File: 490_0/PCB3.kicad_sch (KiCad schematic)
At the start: 7 parts, among them J13 S2B-ZR, J14 Conn_01x08, J22 2000-1-1-20-00-BK, J8 0522711579

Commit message: Changed 8conn and BOM update
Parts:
- J13: footprint S2B-XH-A:JST_S2B-XH-A -> *CapStone*:CONN_S2B-ZR_JST
- J14: footprint *CapStone*:CONN_S8B-XH-A_JST -> *CapStone*:CONN_S08B-XASK-1_JST; Digikey Link https://www.digikey.ca/en/products/detail/jst-sales-america-inc/S8B-XH-A/1651023 -> https://www.digikey.ca/en/products/detail/jst-sales-america-inc/s08b-xask-1/2621356; Manufacturer Part S8B-XH-A -> S08B-XASK-1; Package (none) -> Bulk; Price 0.33 -> 0.81; Supplier P/N 455-S8B-XH-A-ND -> 455-S08B-XASK-1-ND; Type Through Hole -> Through Hole, Right Angle
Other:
- note added: "Camera CSI Connector 1mm pitch, 15-pin FFC"
- note removed: "Camera CSI Connector 0.5mm pitch, 15-pin FFC"
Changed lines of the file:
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@@
 		)
 	)
-	(text "Camera CSI Connector \n0.5mm pitch, 15-pin FFC\n"
+	(text "Camera CSI Connector \n1mm pitch, 15-pin FFC\n"
 		(exclude_from_sim no)
 		(at 33.782 74.168 0)
@@
 			)
 		)
-		(property "Footprint" "S2B-XH-A:JST_S2B-XH-A"
+		(property "Footprint" "*CapStone*:CONN_S2B-ZR_JST"
 			(at 33.655 57.785 0)
 			(effects
@@
 			)
 		)
-		(property "Footprint" "*CapStone*:CONN_S8B-XH-A_JST"
+		(property "Footprint" "*CapStone*:CONN_S08B-XASK-1_JST"
 			(at 198.12 28.575 0)
 			(effects
@@
 			)
 		)
-		(property "Datasheet" "kicad-embed://B3B-XH-A.pdf"
+		(property "Datasheet" "kicad-embed://eXA-WB-new.pdf"
 			(at 198.12 35.56 0)
 			(effects
@@
 			)
 		)
-		(property "Digikey Link" "https://www.digikey.ca/en/products/detail/jst-sales-america-inc/S8B-XH-A/1651023"
+		(property "Digikey Link" "https://www.digikey.ca/en/products/detail/jst-sales-america-inc/s08b-xask-1/2621356"
 			(at 198.12 40.64 0)
 			(effects
@@
 			)
 		)
-		(property "Manufacturer Part" "S8B-XH-A"
+		(property "Manufacturer Part" "S08B-XASK-1"
 			(at 198.12 40.64 0)
 			(effects
@@
 			)
 		)
-		(property "Price" "0.33"
+		(property "Price" "0.81"
 			(at 198.12 40.64 0)
 			(effects
@@
 			)
 		)
-		(property "Supplier P/N" "455-S8B-XH-A-ND"
+		(property "Supplier P/N" "455-S08B-XASK-1-ND"
 			(at 198.12 40.64 0)
 			(effects
@@
 			)
 		)
-		(property "Type" "Through Hole"
+		(property "Type" "Through Hole, Right Angle"
 			(at 198.12 40.64 0)
 			(effects
@@
 			(at 198.12 40.64 0)
 			(effects
+				(font
+					(size 1.27 1.27)
+				)
+				(hide yes)
+			)
+		)
+		(property "Package" "Bulk"
+			(at 198.12 40.64 0)
+			(effects

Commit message: LED names + 5V routing through ESD + renamed ESD chips to "U"
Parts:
- renumbered CR6 to U15
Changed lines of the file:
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@@
 		(dnp no)
 		(fields_autoplaced yes)
-		(property "Reference" "CR6"
+		(property "Reference" "U15"
 			(at 73.66 121.92 0)
 			(effects
@@
 			(project ""
 				(path "/365a82ed-827d-43e1-aa2f-b98221c4179c/a8971e06-9d2b-4df6-83ab-783791bb1c3f"
-					(reference "CR6")
+					(reference "U15")
 					(unit 1)
 				)

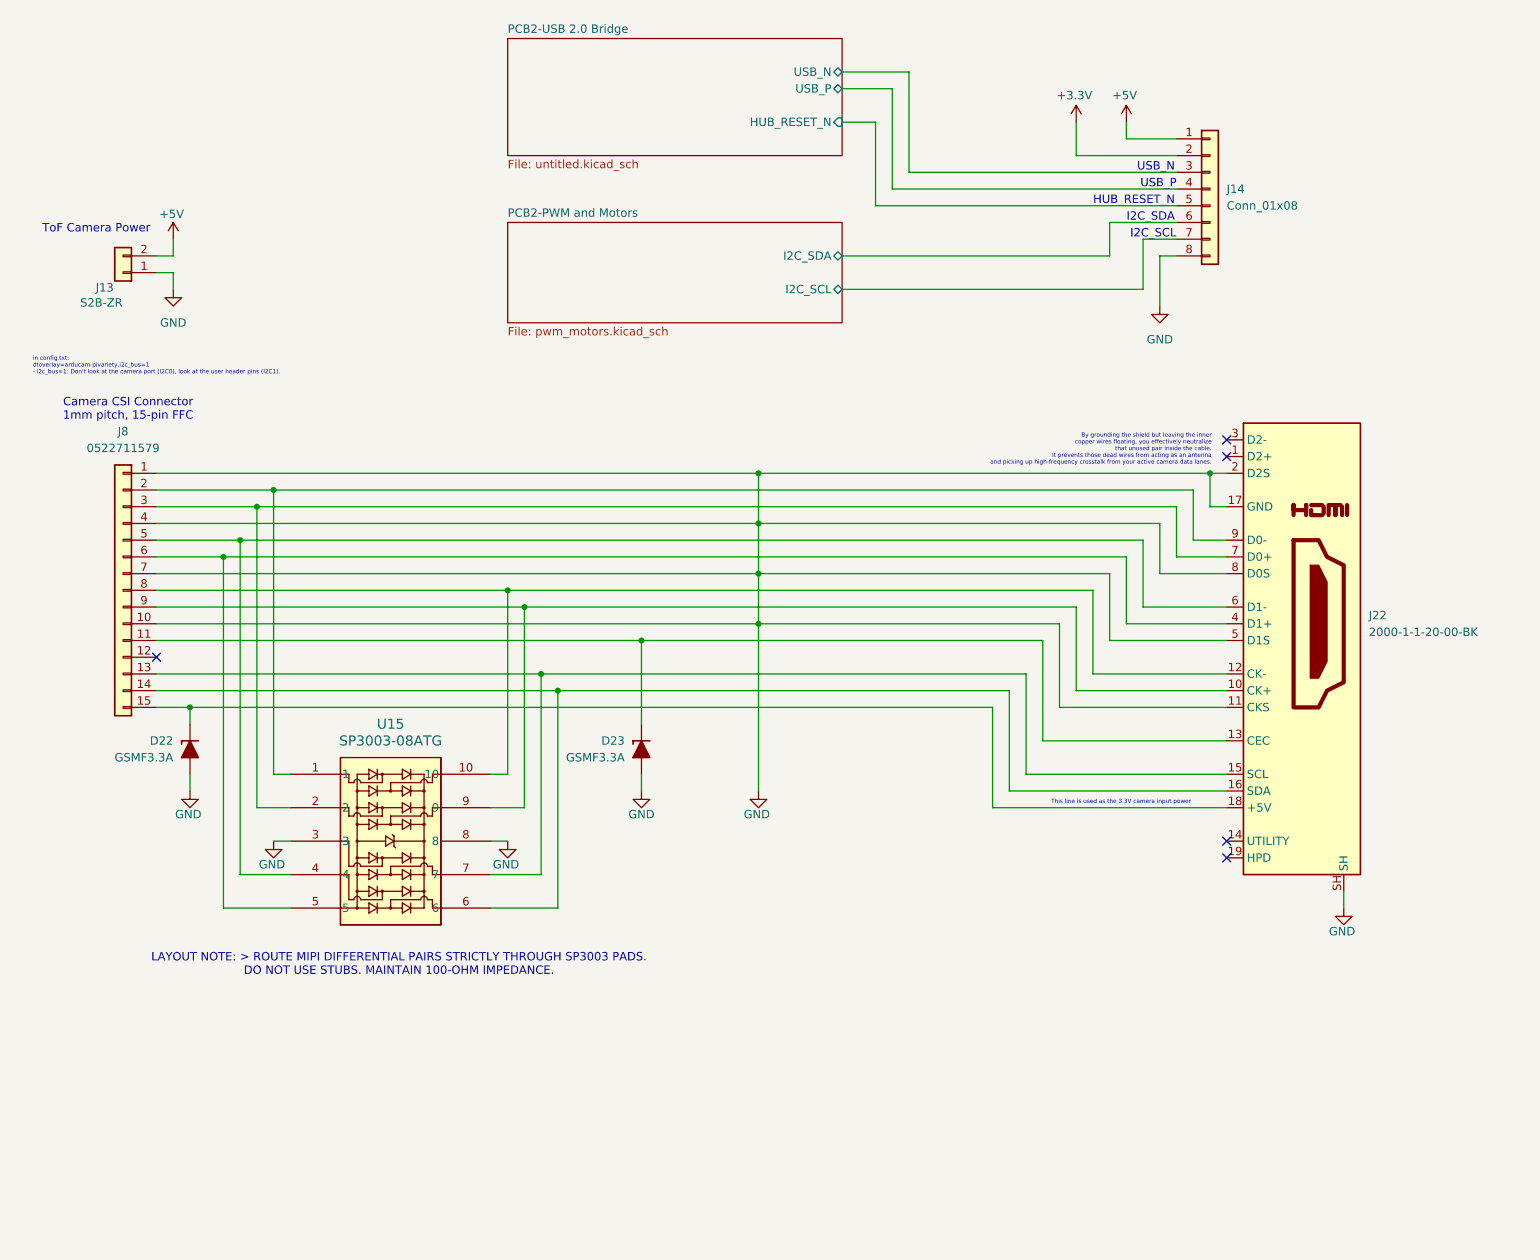
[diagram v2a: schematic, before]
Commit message: Changed ESD chip for HDMI
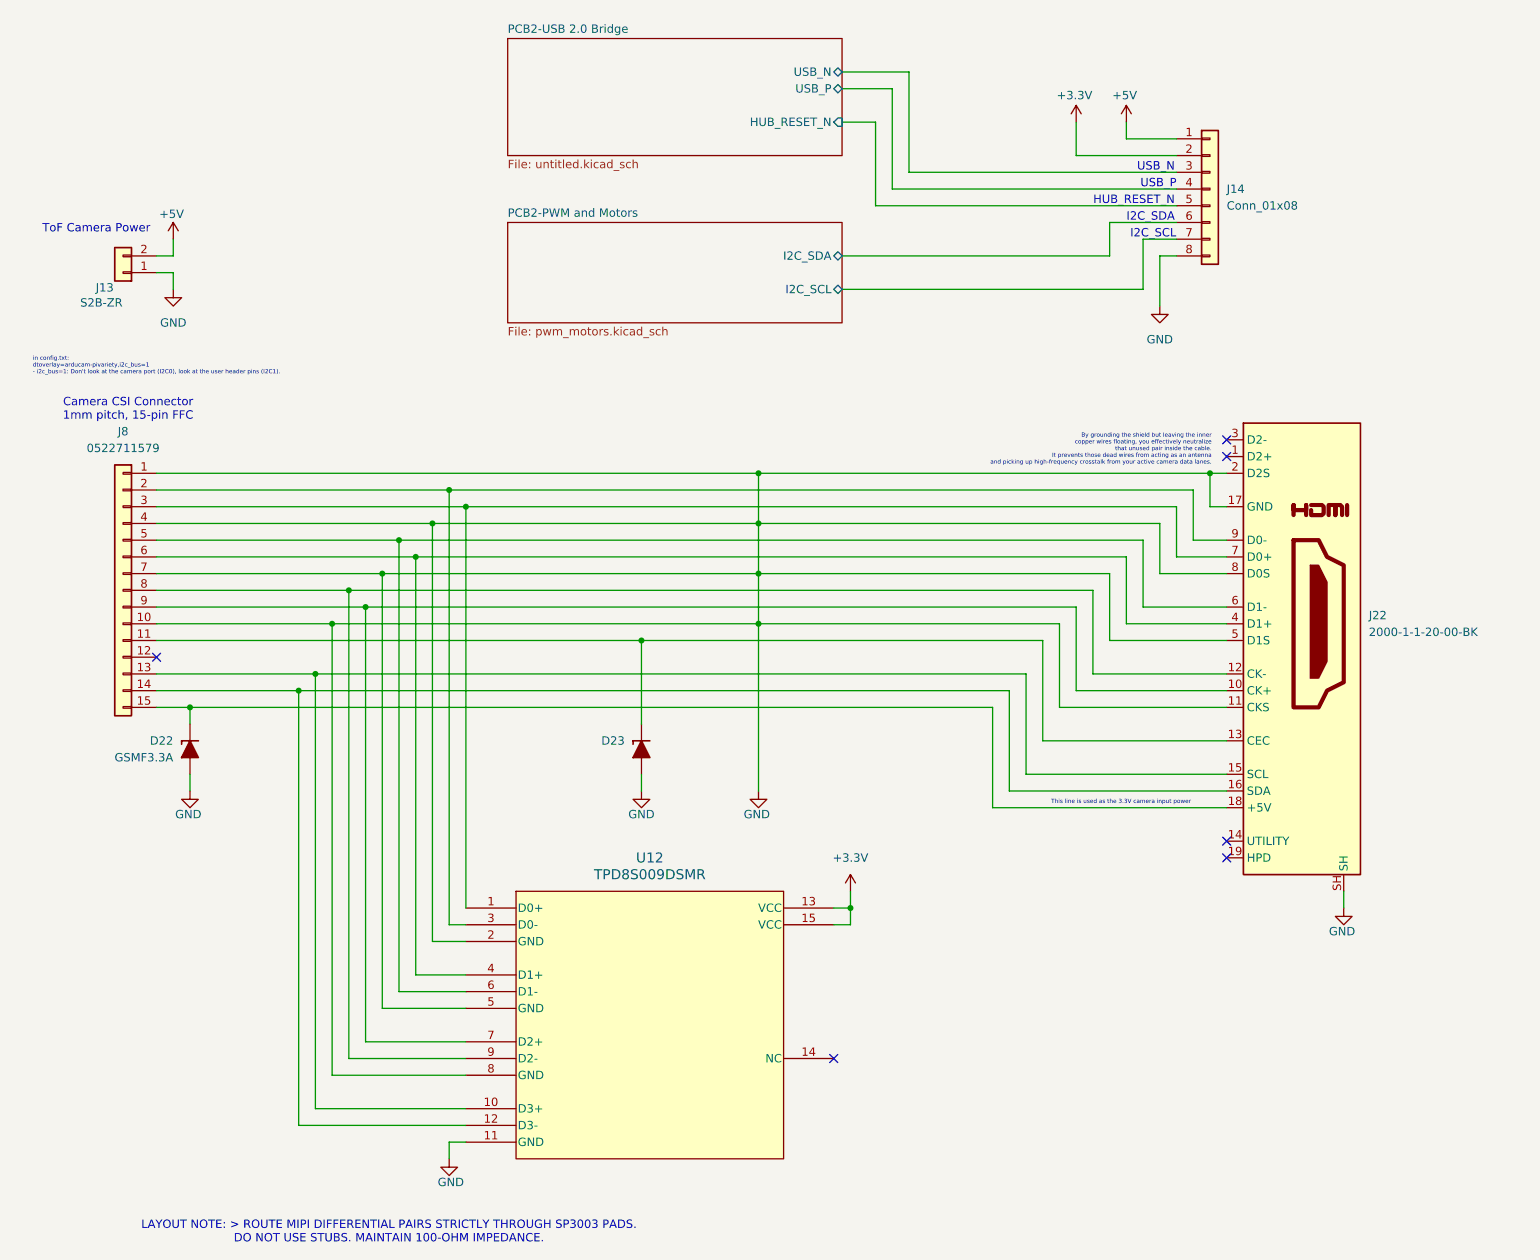
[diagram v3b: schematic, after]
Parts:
- removed U15: SP3003-08ATG, *CapStone*:MSOP10_MO-187_LTF, symbol capstone_parts:SP3003-08ATG
- added U12: TPD8S009DSMR, *CapStone*:TPD8S009DSMR, symbol capstone_parts:TPD8S009DSMR
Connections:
- net +3.3V: now also U12.13 (VCC), U12.15 (VCC)
- net GND: now also U12.11 (GND), U12.2 (GND), U12.5 (GND), U12.8 (GND)
- net at J22.15 (SCL), J8.13 (Pin_13): now also U12.10 (D3+)
- net at J22.16 (SDA), J8.14 (Pin_14): now also U12.12 (D3-)
- net at J22.9 (D0-), J8.2 (Pin_2): now also U12.3 (D0-)
- net at J22.7 (D0+), J8.3 (Pin_3): now also U12.1 (D0+)
- net at J22.6 (D1-), J8.5 (Pin_5): now also U12.6 (D1-)
- net at J22.4 (D1+), J8.6 (Pin_6): now also U12.4 (D1+)
- net at J22.12 (CK-), J8.8 (Pin_8): now also U12.9 (D2-)
- net at J22.10 (CK+), J8.9 (Pin_9): now also U12.7 (D2+)
- no-connect marks 5 -> 6

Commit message: PCB Jumpstart
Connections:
- net GND: now also J22.SH1, J22.SH2, J22.SH3, J22.SH4; no longer J22.SH
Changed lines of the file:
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@@
+	)
+	(junction
+		(at 186.69 134.62)
+		(diameter 0)
+		(color 0 0 0 0)
 	)
 	(junction
@@
 	)
 	(junction
+		(at 217.17 152.4)
+		(diameter 0)
+		(color 0 0 0 0)
+	)
+	(junction
+		(at 214.63 152.4)
+		(diameter 0)
+		(color 0 0 0 0)
+	)
+	(junction
 		(at 198.12 83.82)
 		(diameter 0)
@@
 	)
 	(junction
+		(at 215.9 152.4)
+		(diameter 0)
+		(color 0 0 0 0)
+	)
+	(junction
 		(at 80.01 91.44)
 		(diameter 0)
@@
 	(wire
 		(pts
+			(xy 186.69 134.62) (xy 200.66 134.62)
+		)
+		(stroke
+			(width 0)
+			(type default)
+		)
+	)
+	(wire
+		(pts
 			(xy 64.77 106.68) (xy 129.54 106.68)
 		)
@@
 	(wire
 		(pts
+			(xy 215.9 152.4) (xy 217.17 152.4)
+		)
+		(stroke
+			(width 0)
+			(type default)
+		)
+	)
+	(wire
+		(pts
 			(xy 198.12 83.82) (xy 198.12 88.9)
 		)
@@
 	(wire
 		(pts
+			(xy 217.17 149.86) (xy 217.17 152.4)
+		)
+		(stroke
+			(width 0)
+			(type default)
+		)
+	)
+	(wire
+		(pts
 			(xy 175.26 106.68) (xy 175.26 119.38)
 		)
@@
 	(wire
 		(pts
-			(xy 218.44 149.86) (xy 218.44 147.32)
-		)
-		(stroke
-			(width 0)
-			(type default)
-		)
-	)
-	(wire
-		(pts
 			(xy 38.1 50.8) (xy 40.64 50.8)
 		)
@@
 	(wire
 		(pts
+			(xy 212.09 152.4) (xy 214.63 152.4)
+		)
+		(stroke
+			(width 0)
+			(type default)
+		)
+	)
+	(wire
+		(pts
 			(xy 149.86 25.4) (xy 149.86 40.64)
 		)
@@
 	(wire
 		(pts
+			(xy 214.63 149.86) (xy 214.63 152.4)
+		)
+		(stroke
+			(width 0)
+			(type default)
+		)
+	)
+	(wire
+		(pts
 			(xy 111.76 132.08) (xy 111.76 129.54)
 		)
@@
 	(wire
 		(pts
+			(xy 215.9 154.94) (xy 215.9 152.4)
+		)
+		(stroke
+			(width 0)
+			(type default)
+		)
+	)
+	(wire
+		(pts
 			(xy 140.97 152.4) (xy 143.51 152.4)
 		)
@@
 	(wire
 		(pts
+			(xy 219.71 149.86) (xy 219.71 152.4)
+		)
+		(stroke
+			(width 0)
+			(type default)
+		)
+	)
+	(wire
+		(pts
 			(xy 190.5 99.06) (xy 200.66 99.06)
 		)
@@
 	(wire
 		(pts
+			(xy 212.09 149.86) (xy 212.09 152.4)
+		)
+		(stroke
+			(width 0)
+			(type default)
+		)
+	)
+	(wire
+		(pts
+			(xy 214.63 152.4) (xy 215.9 152.4)
+		)
+		(stroke
+			(width 0)
+			(type default)
+		)
+	)
+	(wire
+		(pts
 			(xy 38.1 119.38) (xy 43.18 119.38)
 		)
@@
 	(wire
 		(pts
+			(xy 219.71 152.4) (xy 217.17 152.4)
+		)
+		(stroke
+			(width 0)
+			(type default)
+		)
+	)
+	(wire
+		(pts
 			(xy 129.54 106.68) (xy 175.26 106.68)
 		)
@@
 	(wire
 		(pts
-			(xy 165.1 134.62) (xy 200.66 134.62)
+			(xy 165.1 134.62) (xy 186.69 134.62)
 		)
 		(stroke
@@
 		(pin "8"
 		)
-		(pin "SH"
+		(pin "SH3"
+		)
+		(pin "SH2"
+		)
+		(pin "SH1"
+		)
+		(pin "SH4"
 		)
 		(instances
@@
 	(symbol
 		(lib_id "power:GND")
-		(at 218.44 149.86 0)
+		(at 215.9 154.94 0)
 		(unit 1)
 		(exclude_from_sim no)
@@
 		(dnp no)
 		(property "Reference" "#PWR0147"
-			(at 218.44 156.21 0)
+			(at 215.9 161.29 0)
 			(effects
 				(font
@@
 		)
 		(property "Value" "GND"
-			(at 218.186 153.416 0)
+			(at 215.646 158.496 0)
 			(effects
 				(font
@@
 		)
 		(property "Footprint" ""
-			(at 218.44 149.86 0)
+			(at 215.9 154.94 0)
 			(effects
 				(font
@@
 		)
 		(property "Datasheet" ""
-			(at 218.44 149.86 0)
+			(at 215.9 154.94 0)
 			(effects
 				(font
@@
 		)
 		(property "Description" "Power symbol creates a global label with name \"GND\" , ground"
-			(at 218.44 149.86 0)
+			(at 215.9 154.94 0)
 			(effects
 				(font
@@
 					(unit 1)
 				)
+			)
+		)
+	)
+	(symbol
+		(lib_id "power:PWR_FLAG")
+		(at 186.69 134.62 180)
+		(unit 1)
+		(exclude_from_sim no)
+		(in_bom yes)
+		(on_board yes)
+		(dnp no)
+		(fields_autoplaced yes)
+		(property "Reference" "#FLG06"
+			(at 186.69 136.525 0)
+			(effects
+				(font
+					(size 1.27 1.27)
+				)
+				(hide yes)
+			)
+		)
+		(property "Value" "PWR_FLAG"
+			(at 186.69 139.7 0)
+			(effects
+				(font
+					(size 1.27 1.27)
+				)
+			)
+		)
+		(property "Footprint" ""
+			(at 186.69 134.62 0)
+			(effects
+				(font
+					(size 1.27 1.27)
+				)
+				(hide yes)
+			)
+		)
+		(property "Datasheet" "~"
+			(at 186.69 134.62 0)
+			(effects
+				(font
+					(size 1.27 1.27)
+				)
+				(hide yes)
+			)
+		)
+		(property "Description" "Special symbol for telling ERC where power comes from"
+			(at 186.69 134.62 0)
+			(effects
+				(font
+					(size 1.27 1.27)
+				)
+				(hide yes)
+			)
+		)
+		(pin "1"
+		)
+		(instances
+			(project ""
+				(path "/365a82ed-827d-43e1-aa2f-b98221c4179c/a8971e06-9d2b-4df6-83ab-783791bb1c3f"
+					(reference "#FLG06")
+					(unit 1)
+				)

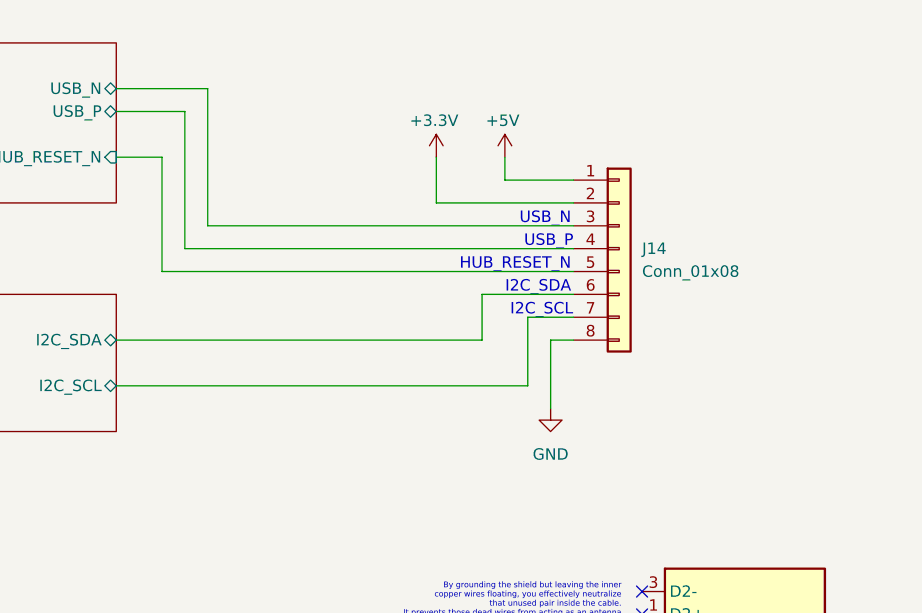
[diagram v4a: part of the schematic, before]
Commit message: Added seperate ground for PWM motors
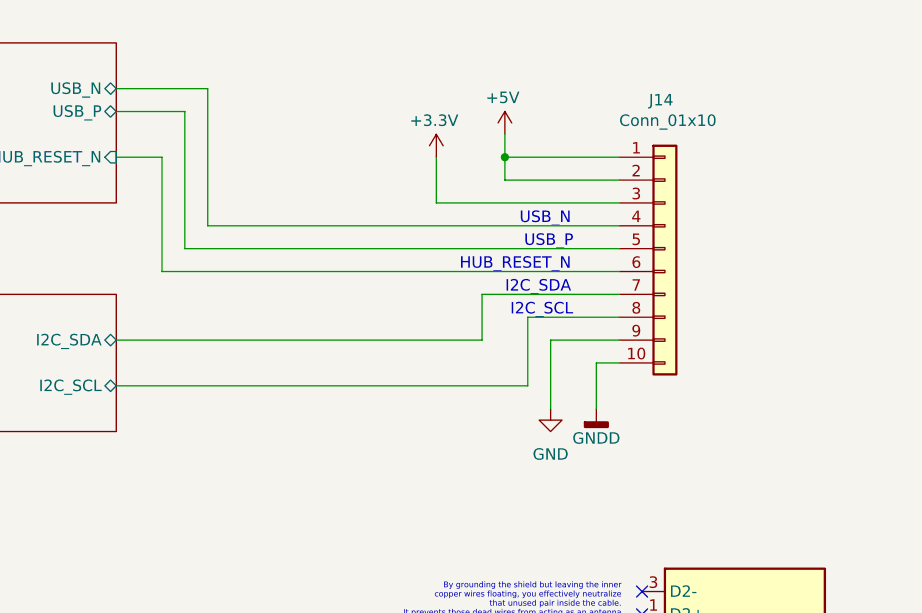
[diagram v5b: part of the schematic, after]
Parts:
- removed J14: Conn_01x08, *CapStone*:CONN_S08B-XASK-1_JST, symbol PCM_4ms_Connector:Conn_01x08
- added J14: Conn_01x10, symbol Connector_Generic:Conn_01x10
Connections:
- net +3.3V: now also J14.3 (Pin_3)
- net +5V: now also J14.1 (Pin_1), J14.2 (Pin_2)
- net GND: now also J14.9 (Pin_9)
- net PCB2-PWM and Motors/I2C_SCL: now also J14.8 (Pin_8)
- net PCB2-PWM and Motors/I2C_SDA: now also J14.7 (Pin_7)
- net PCB2-USB 2.0 Bridge/HUB_RESET_N: now also J14.6 (Pin_6)
- net PCB2-USB 2.0 Bridge/USB_N: now also J14.4 (Pin_4)
- net PCB2-USB 2.0 Bridge/USB_P: now also J14.5 (Pin_5)
- new net GNDD: J14.10 (Pin_10)

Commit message: Added 10 pin connector footprint
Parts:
- J14: footprint (none) -> Connector_JST:JST_XH_S10B-XH-A-1_1x10_P2.50mm_Horizontal
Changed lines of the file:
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@@
 			)
 		)
-		(property "Footprint" ""
+		(property "Footprint" "Connector_JST:JST_XH_S10B-XH-A-1_1x10_P2.50mm_Horizontal"
 			(at 203.2 40.64 0)
 			(effects
